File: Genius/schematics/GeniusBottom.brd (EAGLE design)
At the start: 50 x 100 mm, 160 parts, among them IC1 TL074D, IC10 USBLC6-2SC6, IC2 IS42S16400J, IC3 LM321MF, IC4 CS4271, IC5 NE5532D, IC6 NE5532D, IC7 MIC2005, IC8 STM32H743ZGTx, IC9 N25Q128A13, Q1 SI2309CDS, Q2 2N7002P, Q601 BC846, Q701 BC846, Q801 BC846, Q903 BC846, U4 TLV1117LV, X1 53048-05, X4 FH12-24S-0.5SH, Y1 24.576MHz, Y2 25MHz

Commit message: Rev01 sent for manufacture
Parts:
- IC5, IC6: value NE5532D -> OPA1678IDR
- IC7: value MIC2005 -> MIC2005A-1YM6
- L1, L2: value 1uH -> 10uH
- U4: value TLV1117LV -> TLV1117LV33
- moved C27 7.47 mm to (29.2, 87.9)
- moved C24 2.16 mm to (36.7, 85.6)
- moved L2 2.16 mm to (39.2, 85.6)
- moved C111 0.77 mm to (40.6, 89.9)
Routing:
- net VDDA: track 21.0 -> 19.0 mm
- net N$17: track 6.94 -> 7.77 mm
- net GND: track 193.1 -> 192.6 mm, vias 181 -> 182

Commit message: mostly notes
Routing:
- net ADC0: track 75.6 -> 73.2 mm
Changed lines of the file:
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@@
 <wire x1="19.632" y1="78.95" x2="19.632" y2="79.327" width="0.204" layer="16"/>
 <contactref element="R5" pad="2"/>
-<wire x1="17.653" y1="23.784" x2="17.653" y2="24.892" width="0.2032" layer="1"/>
-<wire x1="17.653" y1="24.892" x2="17.907" y2="25.146" width="0.2032" layer="1"/>
-<wire x1="24.003" y1="25.527" x2="23.749" y2="25.781" width="0.2032" layer="1"/>
-<wire x1="23.749" y1="25.781" x2="18.542" y2="25.781" width="0.2032" layer="1"/>
-<wire x1="17.907" y1="25.146" x2="18.542" y2="25.781" width="0.2032" layer="1"/>
+<wire x1="17.653" y1="23.784" x2="17.653" y2="26.035" width="0.2032" layer="1"/>
+<wire x1="21.844" y1="27.94" x2="19.558" y2="27.94" width="0.2032" layer="1"/>
+<wire x1="17.653" y1="26.035" x2="19.558" y2="27.94" width="0.2032" layer="1"/>
 <wire x1="26.532" y1="54.8" x2="26.532" y2="53.74479375" width="0.2032" layer="15"/>
 <wire x1="26.532" y1="53.74479375" x2="26.7556" y2="53.52119375" width="0.2032" layer="15"/>
 <wire x1="26.7556" y1="53.52119375" x2="26.7556" y2="53.5084" width="0.2032" layer="15"/>
 <wire x1="26.7556" y1="53.5084" x2="27.559" y2="52.705" width="0.2032" layer="15"/>
-<wire x1="27.559" y1="52.705" x2="27.559" y2="27.94" width="0.2032" layer="15"/>
-<wire x1="27.559" y1="27.94" x2="25.146" y2="25.527" width="0.2032" layer="15"/>
-<wire x1="25.146" y1="25.527" x2="24.003" y2="25.527" width="0.2032" layer="15"/>
-<via x="24.003" y="25.527" extent="1-16" drill="0.3048"/>
+<wire x1="27.559" y1="52.705" x2="27.559" y2="32.766" width="0.2032" layer="15"/>
+<wire x1="27.559" y1="32.766" x2="22.733" y2="27.94" width="0.2032" layer="15"/>
+<wire x1="22.733" y1="27.94" x2="21.844" y2="27.94" width="0.2032" layer="15"/>
+<via x="21.844" y="27.94" extent="1-16" drill="0.3048"/>
 </signal>
 <signal name="+12V">
@@
 <wire x1="40.002" y1="18.389" x2="41.487" y2="18.389" width="0.3048" layer="1"/>
 <wire x1="40.002" y1="18.389" x2="39.582" y2="18.389" width="0.204" layer="1"/>
-<wire x1="39.582" y1="18.389" x2="38.732" y2="19.239" width="0.3048" layer="1"/>
-<wire x1="38.732" y1="19.239" x2="38.732" y2="20.929" width="0.3048" layer="1"/>
-<wire x1="38.732" y1="20.929" x2="40.002" y2="22.199" width="0.3048" layer="1"/>
+<wire x1="39.582" y1="18.389" x2="38.986" y2="18.985" width="0.3048" layer="1"/>
+<wire x1="38.986" y1="18.985" x2="38.986" y2="21.183" width="0.3048" layer="1"/>
+<wire x1="38.986" y1="21.183" x2="40.002" y2="22.199" width="0.3048" layer="1"/>
 <wire x1="42.542" y1="23.899" x2="42.122" y2="23.899" width="0.204" layer="1"/>
 <wire x1="40.002" y1="22.199" x2="40.422" y2="22.199" width="0.204" layer="1"/>
@@
 <signal name="OUTR">
 <contactref element="R611" pad="1"/>
-<wire x1="37.792" y1="22.924" x2="38.692" y2="23.824" width="0.3048" layer="1"/>
+<wire x1="38.173" y1="23.305" x2="38.692" y2="23.824" width="0.3048" layer="1"/>
 <wire x1="38.692" y1="23.824" x2="39.927" y2="23.824" width="0.3048" layer="1"/>
 <wire x1="39.927" y1="23.824" x2="40.002" y2="23.899" width="0.204" layer="1"/>
 <contactref element="JP3" pad="1"/>
-<wire x1="37.792" y1="22.924" x2="37.792" y2="13.516" width="0.3048" layer="1"/>
-<wire x1="37.792" y1="13.516" x2="37.846" y2="13.462" width="0.3048" layer="1"/>
-<via x="37.846" y="13.462" extent="1-16" drill="0.3048"/>
-<wire x1="37.846" y1="13.462" x2="37.846" y2="6.454" width="0.3048" layer="15"/>
-<wire x1="37.846" y1="6.454" x2="34.9" y2="3.49" width="0.3048" layer="15"/>
+<wire x1="38.173" y1="23.305" x2="38.173" y2="13.535" width="0.3048" layer="1"/>
+<wire x1="38.1" y1="13.462" x2="38.173" y2="13.535" width="0.3048" layer="1"/>
+<via x="38.1" y="13.462" extent="1-16" drill="0.3048"/>
+<wire x1="38.1" y1="13.462" x2="38.1" y2="6.709553125" width="0.3048" layer="15"/>
+<wire x1="38.1" y1="6.709553125" x2="34.9" y2="3.49" width="0.3048" layer="15"/>
 </signal>
 <signal name="N$36">
@@
 <contactref element="R703" pad="2"/>
 <wire x1="37.05" y1="27.291" x2="34.55" y2="27.291" width="0.204" layer="1"/>
-<wire x1="37.05" y1="27.291" x2="37.084" y2="27.257" width="0.2032" layer="1"/>
-<wire x1="37.084" y1="18.392" x2="34.9" y2="16.19" width="0.2032" layer="1"/>
-<wire x1="37.084" y1="27.257" x2="37.084" y2="18.392" width="0.2032" layer="1"/>
+<wire x1="37.05" y1="27.291" x2="37.211" y2="27.13" width="0.2032" layer="1"/>
+<wire x1="37.211" y1="18.520046875" x2="34.9" y2="16.19" width="0.2032" layer="1"/>
+<wire x1="37.211" y1="27.13" x2="37.211" y2="18.520046875" width="0.2032" layer="1"/>
 <contactref element="JP3" pad="6"/>
 </signal>
@@
 <via x="22.6822" y="52.451" extent="1-16" drill="0.3048"/>
 <wire x1="22.6822" y1="52.451" x2="19.05" y2="48.8188" width="0.2032" layer="15"/>
-<wire x1="19.05" y1="48.8188" x2="19.05" y2="26.67" width="0.2032" layer="15"/>
-<wire x1="14.9" y1="21.27" x2="14.9" y2="22.52" width="0.2032" layer="15"/>
-<wire x1="14.9" y1="22.52" x2="19.05" y2="26.67" width="0.2032" layer="15"/>
+<wire x1="19.05" y1="48.8188" x2="19.05" y2="29.21" width="0.2032" layer="15"/>
+<wire x1="14.9" y1="21.27" x2="14.9" y2="25.06" width="0.2032" layer="15"/>
+<wire x1="14.9" y1="25.06" x2="19.05" y2="29.21" width="0.2032" layer="15"/>
 </signal>
 <signal name="SW_B">
 <contactref element="JP3" pad="8"/>
-<wire x1="28.575" y1="26.289" x2="20.193" y2="26.289" width="0.254" layer="1"/>
-<wire x1="32.004" y1="22.86" x2="28.575" y2="26.289" width="0.254" layer="1"/>
-<wire x1="34.9" y1="21.27" x2="33.292" y2="22.86" width="0.254" layer="1"/>
-<wire x1="33.292" y1="22.86" x2="32.004" y2="22.86" width="0.254" layer="1"/>
-<wire x1="20.193" y1="26.289" x2="19.812" y2="26.67" width="0.254" layer="1"/>
-<via x="19.812" y="26.67" extent="1-16" drill="0.3048"/>
-<wire x1="19.812" y1="26.67" x2="19.812" y2="48.66926875" width="0.2032" layer="15"/>
+<wire x1="29.464" y1="26.162" x2="19.812" y2="26.162" width="0.254" layer="1"/>
+<wire x1="32.131" y1="23.495" x2="29.464" y2="26.162" width="0.254" layer="1"/>
+<wire x1="34.9" y1="21.27" x2="32.6498125" y2="23.495" width="0.254" layer="1"/>
+<wire x1="32.6498125" y1="23.495" x2="32.131" y2="23.495" width="0.254" layer="1"/>
+<via x="19.812" y="26.162" extent="1-16" drill="0.3048"/>
+<wire x1="19.812" y1="26.162" x2="19.812" y2="48.66926875" width="0.2032" layer="15"/>
 <wire x1="19.812" y1="48.66926875" x2="22.591865625" y2="51.449134375" width="0.2032" layer="15"/>
 <via x="23.226865625" y="51.449134375" extent="1-16" drill="0.3048"/>

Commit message: Genius Rev02
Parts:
- R702, R902: value 1k -> 2k
- R704, R904: value 1k -> 10k
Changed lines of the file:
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@@
 <drawing>
 <settings>
-<setting alwaysvectorfont="yes"/>
+<setting alwaysvectorfont="no"/>
 <setting keepoldvectorfont="yes"/>
 <setting verticaltext="up"/>
@@
 <attribute name="NAME" x="35.312" y="28.141" size="0.9" layer="25" font="vector" rot="R270" align="bottom-center"/>
 </element>
-<element name="R704" library="Rebel" library_urn="urn:adsk.eagle:library:15457297" package="0603" package3d_urn="urn:adsk.eagle:package:15457735/3" value="1k" x="37.05" y="28.141" smashed="yes" rot="R270">
+<element name="R704" library="Rebel" library_urn="urn:adsk.eagle:library:15457297" package="0603" package3d_urn="urn:adsk.eagle:package:15457735/3" value="10k" x="37.05" y="28.141" smashed="yes" rot="R270">
 <attribute name="NAME" x="37.939" y="28.141" size="0.9" layer="25" font="vector" rot="R270" align="bottom-center"/>
 </element>
-<element name="R702" library="Rebel" library_urn="urn:adsk.eagle:library:15457297" package="0603" package3d_urn="urn:adsk.eagle:package:15457735/3" value="1k" x="32.05" y="28.141" smashed="yes" rot="R270">
+<element name="R702" library="Rebel" library_urn="urn:adsk.eagle:library:15457297" package="0603" package3d_urn="urn:adsk.eagle:package:15457735/3" value="2k" x="32.05" y="28.141" smashed="yes" rot="R270">
 <attribute name="NAME" x="32.812" y="28.141" size="0.9" layer="25" font="vector" rot="R270" align="bottom-center"/>
 </element>
@@
 <attribute name="NAME" x="27.082" y="28.141" size="0.9" layer="25" font="vector" rot="R270" align="bottom-center"/>
 </element>
-<element name="R904" library="Rebel" library_urn="urn:adsk.eagle:library:15457297" package="0603" package3d_urn="urn:adsk.eagle:package:15457735/3" value="1k" x="28.82" y="28.141" smashed="yes" rot="R270">
+<element name="R904" library="Rebel" library_urn="urn:adsk.eagle:library:15457297" package="0603" package3d_urn="urn:adsk.eagle:package:15457735/3" value="10k" x="28.82" y="28.141" smashed="yes" rot="R270">
 <attribute name="NAME" x="29.582" y="28.141" size="0.9" layer="25" font="vector" rot="R270" align="bottom-center"/>
 </element>
-<element name="R902" library="Rebel" library_urn="urn:adsk.eagle:library:15457297" package="0603" package3d_urn="urn:adsk.eagle:package:15457735/3" value="1k" x="23.82" y="28.141" smashed="yes" rot="R90">
+<element name="R902" library="Rebel" library_urn="urn:adsk.eagle:library:15457297" package="0603" package3d_urn="urn:adsk.eagle:package:15457735/3" value="2k" x="23.82" y="28.141" smashed="yes" rot="R90">
 <attribute name="NAME" x="25.471" y="28.141" size="0.9" layer="25" font="vector" rot="R90" align="bottom-center"/>
 </element>

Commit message: top Rev03 files
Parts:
- added C3: 100n, Rebel:C0603
- added R23: 1k, Rebel:0603
- added R25: 100k, Rebel:0603
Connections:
- new net N$49: C3.1, R23.1, R25.2, R7.1, R9.1
- net +5V: now also R25.1
- net GND: now also C3.2, R23.2; no longer R7.1, R9.1
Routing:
- net GND: track 192.6 -> 191.1 mm, vias 182 -> 180

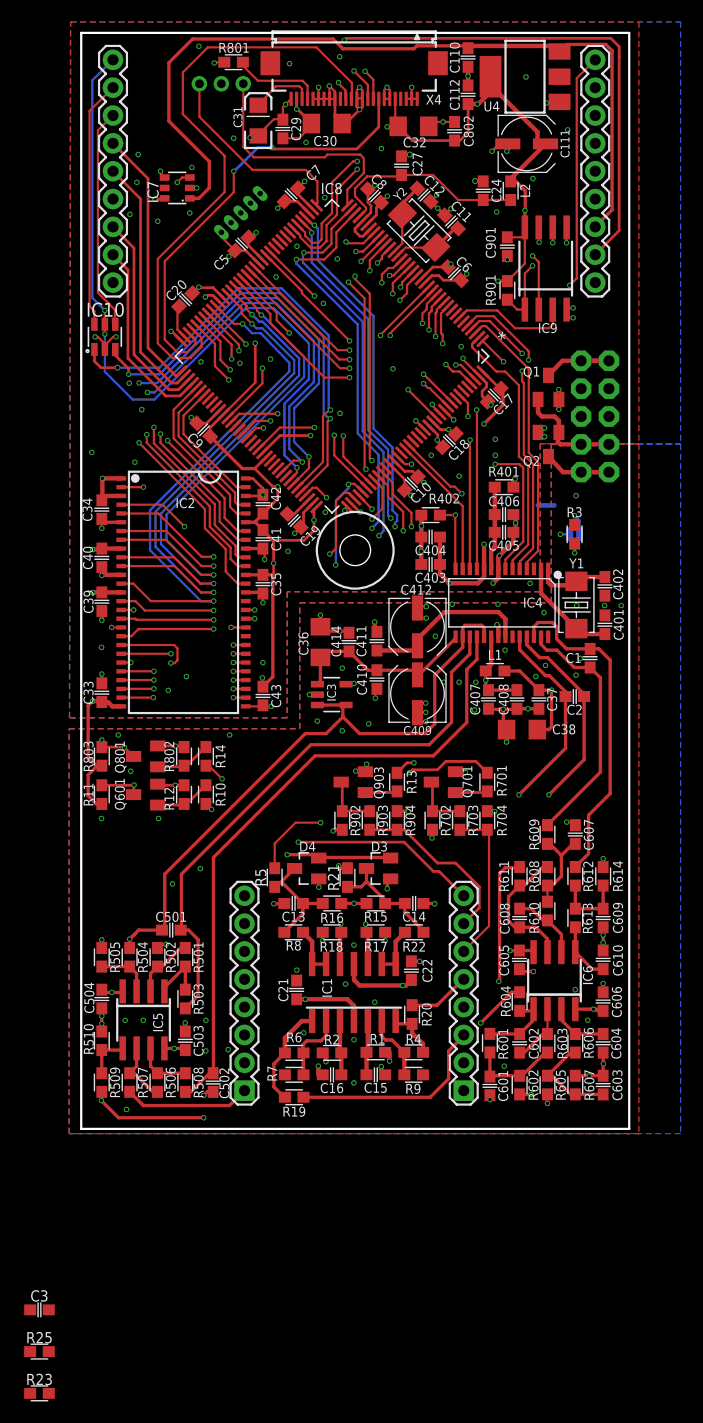
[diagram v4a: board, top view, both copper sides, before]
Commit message: changed input and output filters
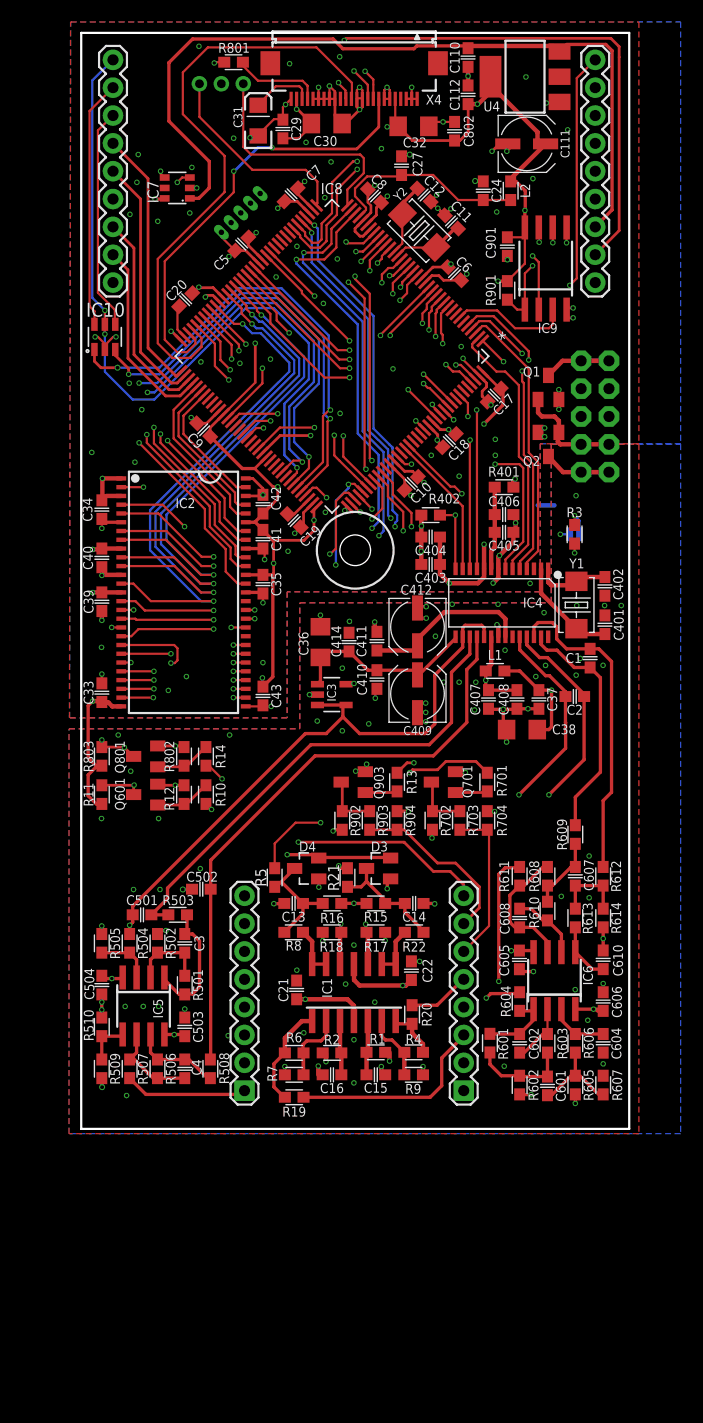
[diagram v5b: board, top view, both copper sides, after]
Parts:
- removed C603, C609: 1n C0G, Rebel:C0603
- removed R23: 1k, Rebel:0603
- removed R25: 100k, Rebel:0603
- added C4: 100p C0G, Rebel:C0603
- C3: value 100n -> 100p C0G
- C601, C607: value 1n C0G -> 480p C0G
- moved C3 36.0 mm to (9.45, 16.9), turned to 90 degrees
- moved C502 17.7 mm to (11.0, 21.9), turned to 180 degrees
- moved R503 7.71 mm to (8.80, 19.5), turned to 180 degrees
- moved C601 5.25 mm to (42.5, 3.92)
- moved R614 3.81 mm to (47.6, 19.2), turned to 270 degrees
- moved C607 3.81 mm to (45.1, 23.0), turned to 90 degrees
- moved C501 3.01 mm to (5.55, 19.5)
- moved R508 2.61 mm to (11.8, 5.48), turned to 90 degrees
- moved R607 2.54 mm to (47.6, 4.00)
- moved R501 2.54 mm to (9.45, 13.1)
- moved R605 2.54 mm to (45.1, 4.00)
- moved R609 2.54 mm to (45.1, 26.9)
- moved R612 2.54 mm to (47.6, 23.0)
- moved C503 1.27 mm to (9.45, 9.31)
- moved R510 1.27 mm to (1.88, 9.31)
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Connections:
- removed net N$49: C3.1, R23.1, R25.2, R7.1, R9.1
- net +5V: no longer R25.1
- net GND: now also R7.1, R9.1; no longer C3.2, C601.1, C603.2, C607.1, C609.2, R23.2
- net N$1: now also C601.1; no longer C603.1
- net N$25: now also C607.1; no longer C609.1
- net N$38: now also C3.1
- net N$40: now also C3.2
- net N$43: now also C4.1
- net N$45: now also C4.2
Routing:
- net GND: track 191.1 -> 180.7 mm, vias 180 -> 182
- net CS_VREF: track 88.6 -> 79.2 mm, vias 4 -> 3
- net AINA: track 53.0 -> 45.3 mm
- net N$40: track 5.22 -> 11.9 mm
- net AINB: track 59.4 -> 55.0 mm
- net N$45: track 5.07 -> 8.08 mm
- net N$43: track 5.77 -> 8.28 mm
- net N$26: track 8.42 -> 6.83 mm
- net N$38: track 5.77 -> 7.13 mm
- net N$17: track 7.77 -> 6.55 mm
- net AOUTA+: track 47.4 -> 48.4 mm
- net AOUTB-: track 22.8 -> 21.8 mm
- net OUTL: track 8.98 -> 10.0 mm
- net AOUTB+: track 30.3 -> 29.3 mm
- net +12V: track 99.2 -> 98.5 mm
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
